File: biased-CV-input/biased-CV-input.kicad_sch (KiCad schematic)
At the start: 14 parts, among them J1 3.5mm_Mono_Switched, J2 Conn_01x04, U1 TLV9061xDBV

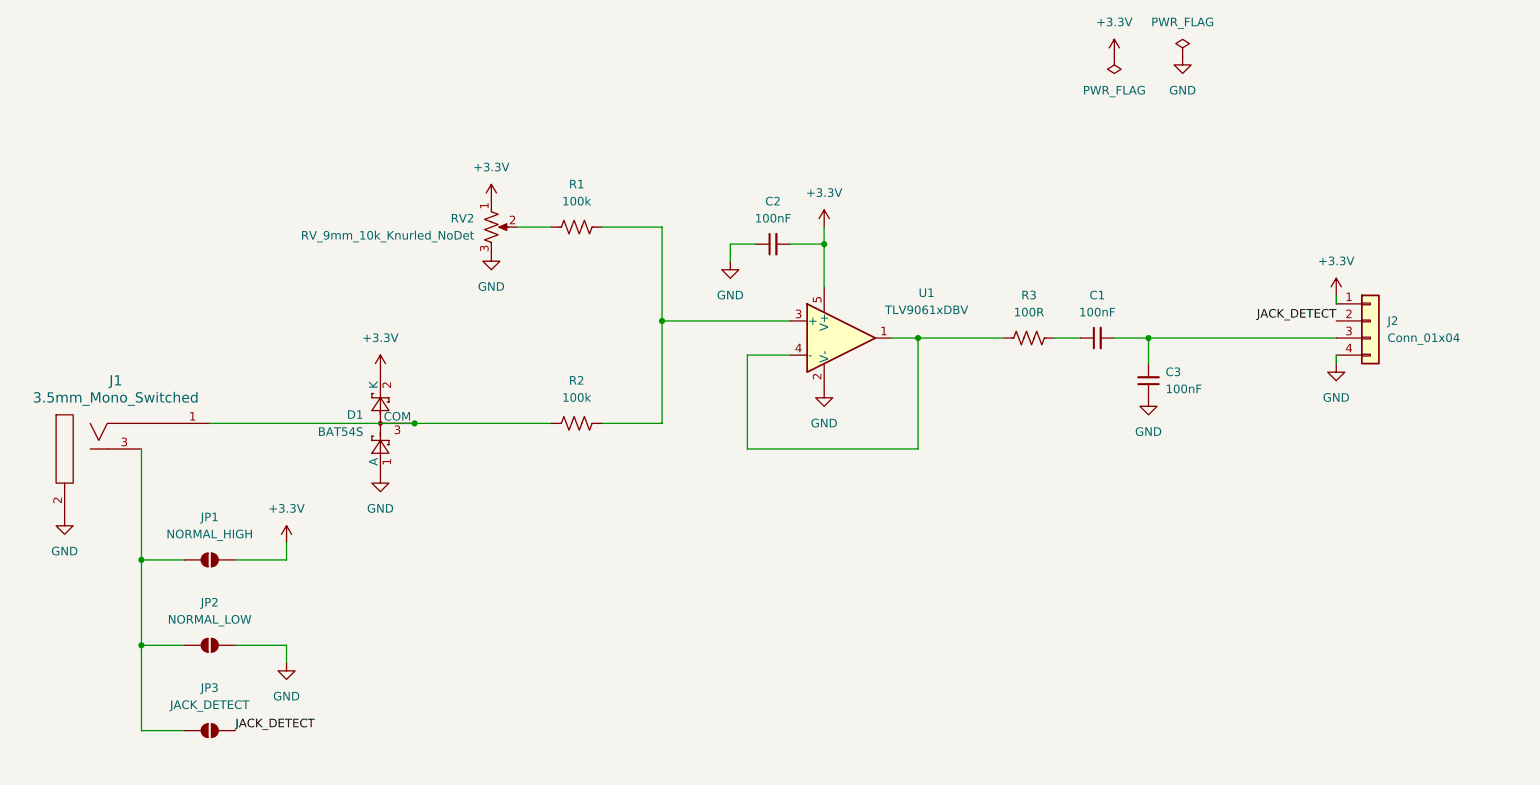
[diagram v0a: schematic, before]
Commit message: Update biased-CV-input.kicad_sch
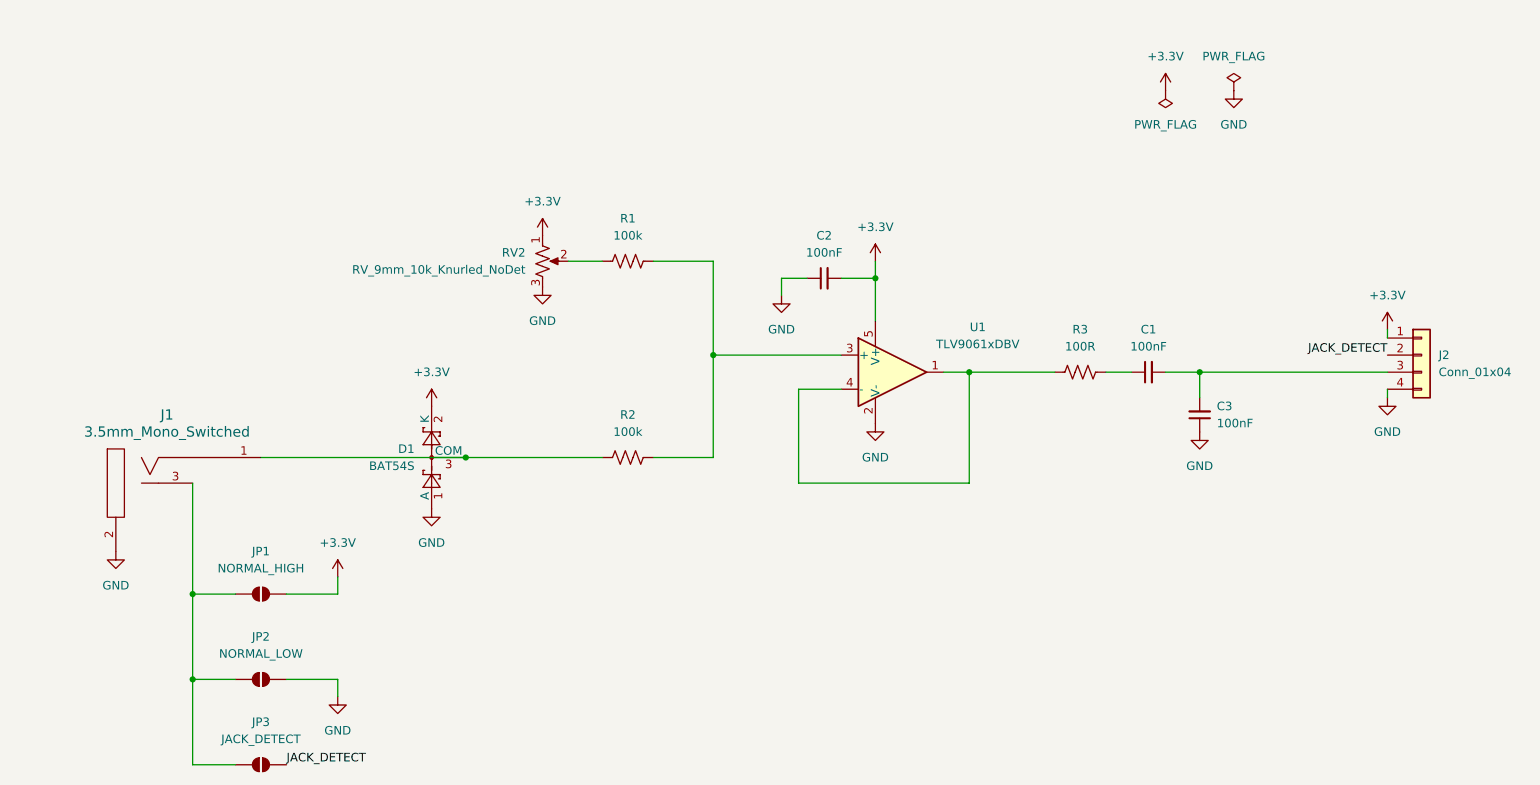
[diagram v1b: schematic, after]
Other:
- company: (none) -> github.com/brianvarren/patch_bits
- moved on the sheet: C1, C2, C3, D1, J1, J2, JP1, JP2, JP3, R1, R2, R3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
